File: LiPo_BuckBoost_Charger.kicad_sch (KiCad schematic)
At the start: 61 parts, among them J2 Type-C_6P, J3 Conn_01x01, J4 Conn_01x01, J7 JST PH Connector, Q1 SI2301, Q2 SI2301, U1 TP4056, U2 DW01A, U3 FS8205A, U4 TPS63020

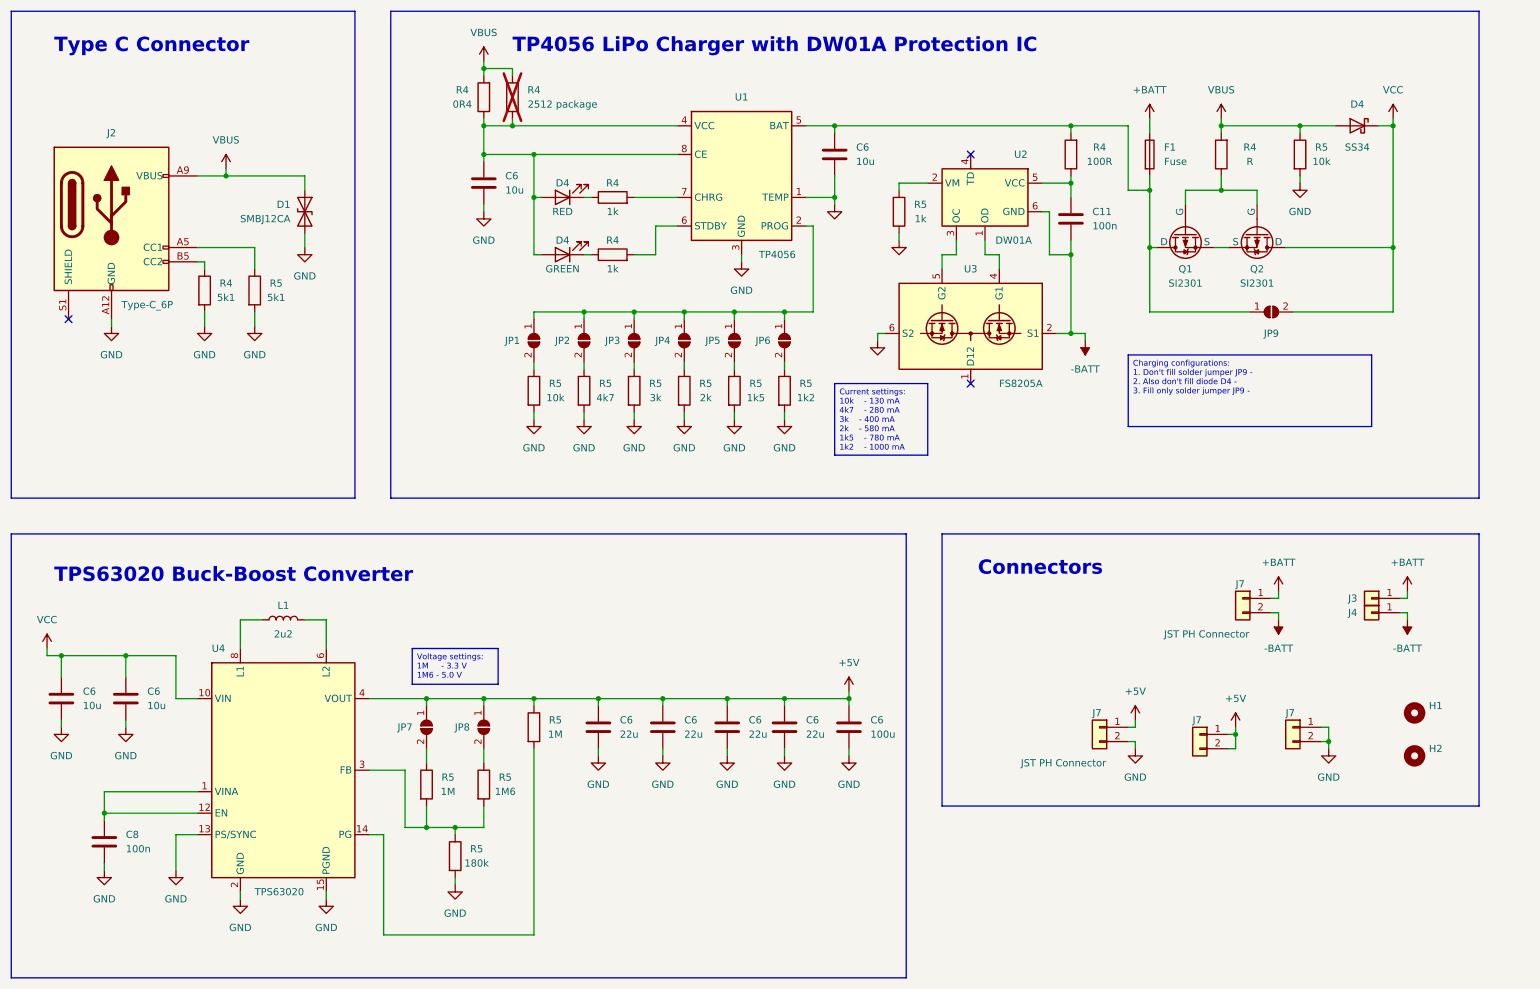
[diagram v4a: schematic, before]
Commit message: version 1.3 - added circuit which disconnects battery from load during charging
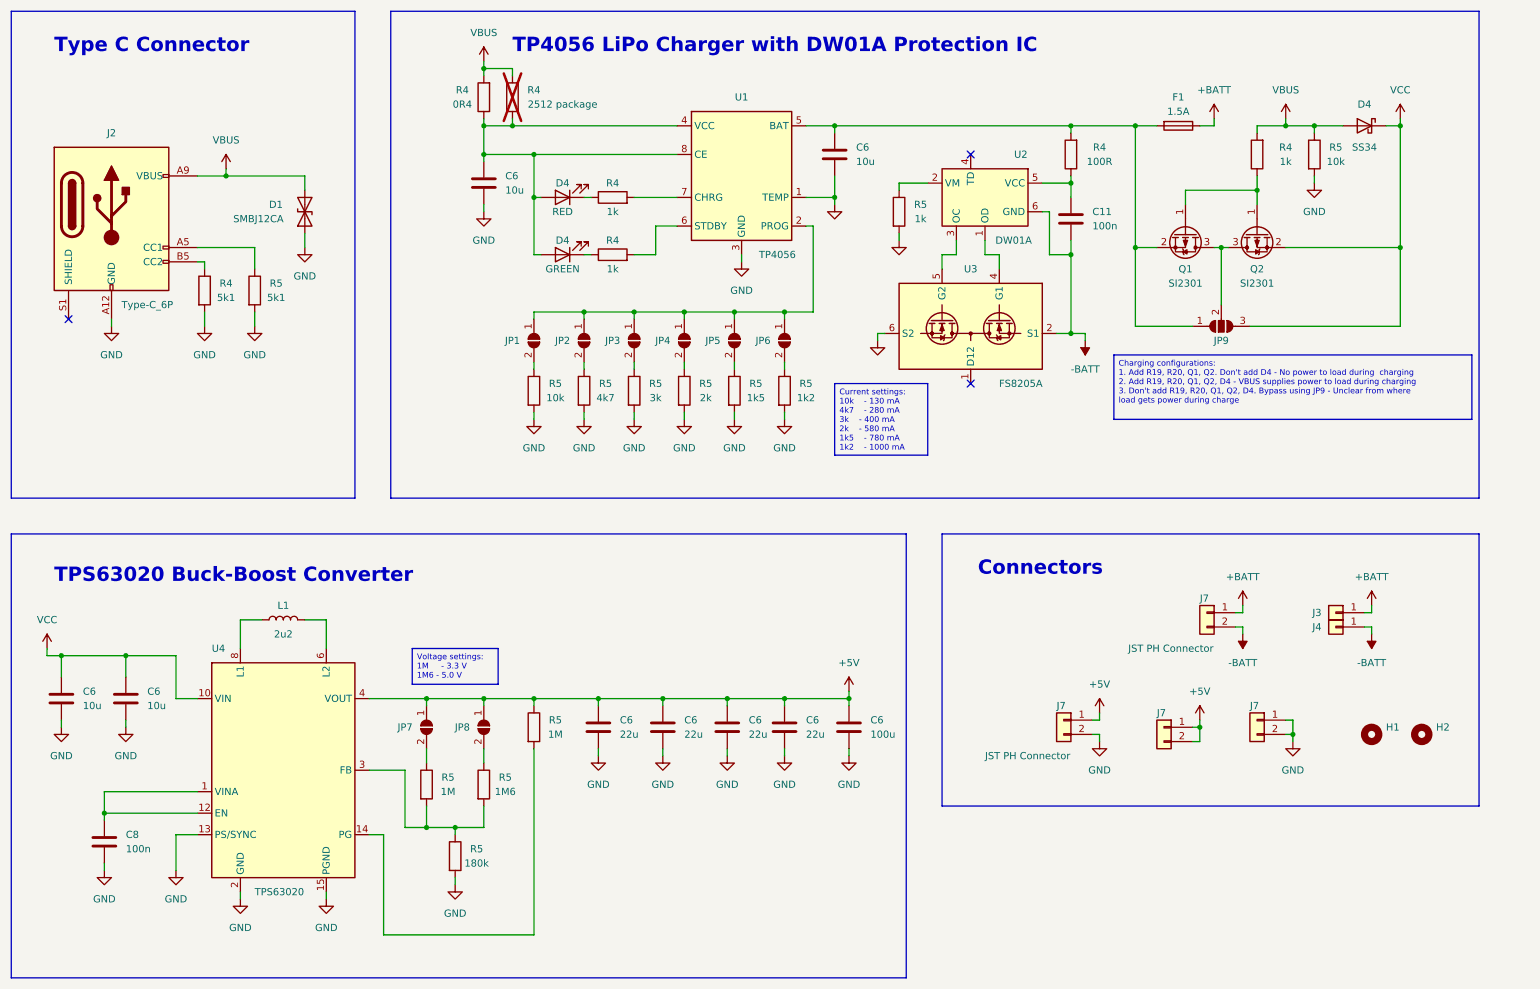
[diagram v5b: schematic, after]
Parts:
- removed JP9: SolderJumper_2_Open, Jumper:SolderJumper-2_P1.3mm_Open_TrianglePad1.0x1.5mm, symbol Jumper:SolderJumper_2_Open
- removed Q1, Q2: SI2301, Package_TO_SOT_SMD:SOT-23, symbol Simulation_SPICE:PMOS
- added JP9: SolderJumper_3_Open, symbol Jumper:SolderJumper_3_Open
- added Q1, Q2: SI2301, Package_TO_SOT_SMD:SOT-23, symbol Device:Q_PMOS_GSD
- F1: value Fuse -> 1.5A; footprint (none) -> Fuse:Fuse_1206_3216Metric
- R4: value R -> 1k
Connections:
- net GND: now also D1.1 (A1); no longer D1.2 (A2)
- net VBUS: now also D1.2 (A2); no longer D1.1 (A1)
- net VCC: now also JP9.3 (B), Q2.2 (S)
- net at C6.1, F1.2, R4.2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: now also JP9.1 (A), Q1.2 (S)
- net at R4.1: now also Q1.1 (G), Q2.1 (G)
- new net: JP9.2 (C), Q1.3 (D), Q2.3 (D)
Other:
- moved on the sheet: D1, D4, F1, H1, H2, J3, J4, J7, R4, R5
